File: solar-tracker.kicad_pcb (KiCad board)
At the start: 2 copper layers, 25 parts, among them J1 LDR1, J2 LDR2, J3 Motor, J4 Power, Q1 TIP41C, Q2 TIP41C, Q3 TIP42C, Q4 TIP42C, U1 LM324

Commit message: Create PCB layout for blocks
Signed-off-by: Sam Protsenko <joe.skb7@gmail.com>
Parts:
- removed the REF** at (27.9, 25.4)
- removed the REF** at (273.1, 24.1)
- removed the REF** at (25.4, 153.7)
- removed the REF** at (274.3, 153.7)
- added REF**: 1pin, Connectors:1pin, F.Cu at (106.7, 34.3)
- added REF**: 1pin, Connectors:1pin, F.Cu at (228.6, 26.7)
- added REF**: 1pin, Connectors:1pin, F.Cu at (105.4, 163.8)
- added REF**: 1pin, Connectors:1pin, F.Cu at (251.5, 157.5)
- moved J4 116.9 mm to (262.9, 100.3), turned to 90 degrees
- moved D1 101.1 mm to (228.6, 74.9)
- moved D2 101.1 mm to (246.4, 74.9)
- moved Q2 100.6 mm to (254.0, 77.5)
- moved Q4 100.6 mm to (254.0, 118.1)
- moved J3 100.6 mm to (234.9, 97.8)
- moved Q1 100.6 mm to (221.0, 77.5)
- moved Q3 100.6 mm to (221.0, 118.1)
- moved D3 100.4 mm to (228.6, 105.4)
- moved D4 100.4 mm to (246.4, 105.4)
- moved RV2 81.6 mm to (61.0, 105.4), turned to 90 degrees
- moved RV1 78.2 mm to (61.0, 91.4), turned to 90 degrees
- moved R1 77.5 mm to (68.6, 88.9)
- moved R3 74.4 mm to (121.9, 116.8), turned to 90 degrees
- moved R2 70.3 mm to (68.6, 102.9)
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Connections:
- J4 pad 1: VCC -> GND
- J4 pad 2: GND -> VCC
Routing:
- net GND: track 33.0 -> 222.0 mm
- net VCC: track 33.0 -> 208.3 mm
- net Net-(Q2-Pad1): track 47.8 -> 186.7 mm, vias 0 -> 4
- net Net-(J1-Pad2): track 0.00 -> 64.5 mm, vias 0 -> 2
- net Net-(Q1-Pad1): track 47.8 -> 92.9 mm, vias 0 -> 2
- net Net-(R1-Pad2): track 0.00 -> 27.5 mm
- net Net-(R2-Pad1): track 0.00 -> 27.5 mm
- net Net-(C2-Pad1): track 0.00 -> 26.7 mm
- net Net-(R1-Pad1): track 0.00 -> 12.1 mm
- net Net-(D2-Pad2): track 49.6 -> 59.8 mm
- net Net-(D1-Pad2): track 49.5 -> 59.7 mm
- net Net-(U1-Pad8): track 0.00 -> 2.54 mm
- net Net-(U1-Pad13): track 0.00 -> 2.54 mm
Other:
- net class Default: clearance 0.5 -> 0.3; via_dia 1.2 -> 2.5; via_drill 0.8 -> 1
- net class Power removed
- rule trace_clearance: 0.5 -> 0.3

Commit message: Finish PCB
Signed-off-by: Sam Protsenko <joe.skb7@gmail.com>
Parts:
- moved REF** 150.8 mm to (127.0, 72.4)
- moved D1 148.2 mm to (88.9, 25.4)
- moved D2 148.2 mm to (106.7, 25.4)
- moved D3 148.2 mm to (88.9, 55.9)
- moved D4 148.2 mm to (106.7, 55.9)
- moved J3 148.2 mm to (95.2, 48.3)
- moved J4 148.2 mm to (123.2, 50.8)
- moved Q1 148.2 mm to (81.3, 27.9)
- moved Q2 148.2 mm to (114.3, 27.9)
- moved Q3 148.2 mm to (81.3, 68.6)
- moved Q4 148.2 mm to (114.3, 68.6)
- moved REF** 125.8 mm to (19.1, 72.4)
- moved REF** 101.7 mm to (127.0, 21.6)
- moved REF** 88.5 mm to (19.1, 21.6)
- moved C1 79.0 mm to (52.1, 62.2)
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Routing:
- net Net-(Q2-Pad1): track 186.7 -> 208.2 mm
- net VCC: track 208.3 -> 221.0 mm
- net GND: track 222.0 -> 232.6 mm
- net Net-(Q1-Pad1): track 92.9 -> 94.5 mm

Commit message: pcb: Add PCB edges and copper pour
Signed-off-by: Sam Protsenko <joe.skb7@gmail.com>
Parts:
- moved ? 2.54 mm to (19.1, 69.8)
- moved C2 2.54 mm to (67.3, 41.9)
- moved REF** 2.54 mm to (127.0, 69.8)
- moved Q1 2.54 mm to (81.3, 25.4)
- moved Q2 2.54 mm to (114.3, 25.4)
- moved C1 2.54 mm to (52.1, 59.7)
- moved D1 2.54 mm to (88.9, 22.9)
- moved D2 2.54 mm to (106.7, 22.9)
- moved D3 2.54 mm to (88.9, 53.3)
- moved D4 2.54 mm to (106.7, 53.3)
- moved J1 2.54 mm to (22.9, 34.3)
- moved J2 2.54 mm to (22.9, 48.3)
- moved J3 2.54 mm to (95.2, 45.7)
- moved J4 2.54 mm to (123.2, 48.3)
- moved R1 2.54 mm to (39.4, 31.8)
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- renumbered REF** to ?
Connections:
- ? pad : (no net) -> GND
- REF** pad : (no net) -> GND (x3)
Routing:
- added copper zone on B.Cu, net GND
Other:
- board outline added: 115.6 x 58.4 mm

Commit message: pcb: Reduce via size
Signed-off-by: Sam Protsenko <joe.skb7@gmail.com>
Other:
- net class Default: via_dia 2.5 -> 2
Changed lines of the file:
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@@
     (links 51)
     (no_connects 0)
-    (area 15.24 14.927 130.810001 74.025)
+    (area 15.189999 14.927 130.860001 74.025)
     (thickness 1.6)
     (drawings 4)
@@
     (0 F.Cu signal)
     (31 B.Cu signal)
-    (33 F.Adhes user)
-    (35 F.Paste user)
+    (33 F.Adhes user hide)
+    (35 F.Paste user hide)
     (37 F.SilkS user)
-    (39 F.Mask user)
-    (40 Dwgs.User user)
-    (41 Cmts.User user)
-    (42 Eco1.User user)
-    (43 Eco2.User user)
+    (39 F.Mask user hide)
+    (40 Dwgs.User user hide)
+    (41 Cmts.User user hide)
+    (42 Eco1.User user hide)
+    (43 Eco2.User user hide)
     (44 Edge.Cuts user)
-    (45 Margin user)
+    (45 Margin user hide)
     (47 F.CrtYd user)
-    (49 F.Fab user)
+    (49 F.Fab user hide)
   )
   (setup
@@
     (segment_width 0.2)
     (edge_width 0.1)
-    (via_size 2.5)
+    (via_size 2)
     (via_drill 1)
     (via_min_size 0.4)
@@
     (visible_elements FFFFEF7F)
     (pcbplotparams
-      (layerselection 0x00030_80000001)
+      (layerselection 0x00020_80000001)
       (usegerberextensions false)
       (excludeedgelayer true)
@@
       (outputformat 1)
       (mirror false)
-      (drillshape 1)
+      (drillshape 0)
       (scaleselection 1)
-      (outputdirectory ""))
+      (outputdirectory ./))
   )
   (net 0 "")
@@
     (clearance 0.3)
     (trace_width 0.5)
-    (via_dia 2.5)
+    (via_dia 2)
     (via_drill 1)
     (uvia_dia 0.3)
@@
     (add_net "Net-(U1-Pad8)")
     (add_net VCC)
+  )
+  (module Connectors:1pin (layer F.Cu)
+    (at 19.05 19.05)
+    (descr "module 1 pin (ou trou mecanique de percage)")
+    (tags DEV)
+    (fp_text reference REF** (at 0 -3.048) (layer F.SilkS) hide
+      (effects (font (size 1 1) (thickness 0.15)))
+    )
+    (fp_text value 1pin (at 0 3) (layer F.Fab) hide
+      (effects (font (size 1 1) (thickness 0.15)))
+    )
+    (fp_circle (center 0 0) (end 2 0.8) (layer F.Fab) (width 0.1))
+    (fp_circle (center 0 0) (end 2.6 0) (layer F.CrtYd) (width 0.05))
+    (fp_circle (center 0 0) (end 0 -2.286) (layer F.SilkS) (width 0.12))
+    (pad "" thru_hole circle (at 0 0) (size 5 5) (drill 3.2) (layers *.Cu *.Mask)
+      (net 2 GND))
   )
   (module Housings_DIP:DIP-14_W7.62mm (layer F.Cu)
@@
   )
   (module Connectors:1pin (layer F.Cu)
-    (at 19.05 19.05)
-    (descr "module 1 pin (ou trou mecanique de percage)")
-    (tags DEV)
-    (fp_text reference REF** (at 0 -3.048) (layer F.SilkS) hide
-      (effects (font (size 1 1) (thickness 0.15)))
-    )
-    (fp_text value 1pin (at 0 3) (layer F.Fab) hide
-      (effects (font (size 1 1) (thickness 0.15)))
-    )
-    (fp_circle (center 0 0) (end 2 0.8) (layer F.Fab) (width 0.1))
-    (fp_circle (center 0 0) (end 2.6 0) (layer F.CrtYd) (width 0.05))
-    (fp_circle (center 0 0) (end 0 -2.286) (layer F.SilkS) (width 0.12))
-    (pad "" thru_hole circle (at 0 0) (size 5 5) (drill 3.2) (layers *.Cu *.Mask)
-      (net 2 GND))
-  )
-  (module Connectors:1pin (layer F.Cu)
     (at 127 19.05)
     (descr "module 1 pin (ou trou mecanique de percage)")
@@
   (segment (start 50.8 44.45) (end 46.99 44.45) (width 0.5) (layer B.Cu) (net 6))
   (segment (start 46.99 52.07) (end 50.8 52.07) (width 0.5) (layer B.Cu) (net 6))
-  (via (at 46.99 52.07) (size 2.5) (drill 1) (layers F.Cu B.Cu) (net 6))
+  (via (at 46.99 52.07) (size 2) (drill 1) (layers F.Cu B.Cu) (net 6))
   (segment (start 46.99 44.45) (end 46.99 52.07) (width 0.5) (layer F.Cu) (net 6))
-  (via (at 46.99 44.45) (size 2.5) (drill 1) (layers F.Cu B.Cu) (net 6))
+  (via (at 46.99 44.45) (size 2) (drill 1) (layers F.Cu B.Cu) (net 6))
   (segment (start 43.18 36.83) (end 43.18 36.83) (width 0.5) (layer B.Cu) (net 6))
   (segment (start 22.86 43.18) (end 33.02 43.18) (width 0.5) (layer B.Cu) (net 6))
@@
   (segment (start 46.99 27.94) (end 46.99 39.37) (width 0.5) (layer F.Cu) (net 7))
   (segment (start 77.47 27.94) (end 68.58 27.94) (width 0.5) (layer B.Cu) (net 7))
-  (via (at 46.99 39.37) (size 2.5) (drill 1) (layers F.Cu B.Cu) (net 7))
-  (via (at 46.99 27.94) (size 2.5) (drill 1) (layers F.Cu B.Cu) (net 7))
+  (via (at 46.99 39.37) (size 2) (drill 1) (layers F.Cu B.Cu) (net 7))
+  (via (at 46.99 27.94) (size 2) (drill 1) (layers F.Cu B.Cu) (net 7))
   (segment (start 46.99 39.37) (end 50.8 39.37) (width 0.5) (layer B.Cu) (net 7))
   (segment (start 46.99 27.94) (end 68.58 27.94) (width 0.5) (layer B.Cu) (net 7))
@@
   (segment (start 49.53 55.88) (end 49.53 63.5) (width 0.5) (layer B.Cu) (net 8))
   (segment (start 49.53 63.5) (end 50.8 64.77) (width 0.5) (layer B.Cu) (net 8))
-  (via (at 67.31 64.77) (size 2.5) (drill 1) (layers F.Cu B.Cu) (net 8))
+  (via (at 67.31 64.77) (size 2) (drill 1) (layers F.Cu B.Cu) (net 8))
   (segment (start 50.8 64.77) (end 67.31 64.77) (width 0.5) (layer B.Cu) (net 8))
   (segment (start 67.31 64.77) (end 73.66 64.77) (width 0.5) (layer F.Cu) (net 8))
-  (via (at 73.66 64.77) (size 2.5) (drill 1) (layers F.Cu B.Cu) (net 8))
-  (via (at 73.66 33.02) (size 2.5) (drill 1) (layers F.Cu B.Cu) (net 8))
+  (via (at 73.66 64.77) (size 2) (drill 1) (layers F.Cu B.Cu) (net 8))
+  (via (at 73.66 33.02) (size 2) (drill 1) (layers F.Cu B.Cu) (net 8))
   (segment (start 125.73 26.67) (end 118.11 19.05) (width 0.5) (layer B.Cu) (net 8))
   (segment (start 125.73 27.305332) (end 125.73 26.67) (width 0.5) (layer B.Cu) (net 8))
@@
   (segment (start 119.38 45.72) (end 125.73 45.72) (width 0.5) (layer B.Cu) (net 8))
   (segment (start 118.11 19.05) (end 73.66 19.05) (width 0.5) (layer B.Cu) (net 8))
-  (via (at 73.66 19.05) (size 2.5) (drill 1) (layers F.Cu B.Cu) (net 8))
+  (via (at 73.66 19.05) (size 2) (drill 1) (layers F.Cu B.Cu) (net 8))
   (segment (start 73.66 19.05) (end 73.66 33.02) (width 0.5) (layer F.Cu) (net 8))
   (segment (start 119.38 45.72) (end 119.38 63.5) (width 0.5) (layer B.Cu) (net 8))

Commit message: pcb: Remove copper pour
Prepare PCB for LUT (toner transfer method).

Signed-off-by: Sam Protsenko <joe.skb7@gmail.com>
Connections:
- ? pad : GND -> (no net)
- REF** pad : GND -> (no net) (x3)
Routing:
- removed copper zone on B.Cu, net GND
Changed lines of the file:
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@@
 (kicad_pcb (version 4) (host pcbnew 4.0.7+dfsg1-1)
   (general
-    (links 51)
+    (links 47)
     (no_connects 0)
-    (area 15.189999 14.927 130.860001 74.025)
+    (area 15.189999 15.189999 130.860001 73.710001)
     (thickness 1.6)
     (drawings 4)
@@
       (padsonsilk false)
       (subtractmaskfromsilk false)
-      (outputformat 1)
+      (outputformat 5)
       (mirror false)
       (drillshape 0)
@@
     (fp_circle (center 0 0) (end 2.6 0) (layer F.CrtYd) (width 0.05))
     (fp_circle (center 0 0) (end 0 -2.286) (layer F.SilkS) (width 0.12))
-    (pad "" thru_hole circle (at 0 0) (size 5 5) (drill 3.2) (layers *.Cu *.Mask)
-      (net 2 GND))
+    (pad "" thru_hole circle (at 0 0) (size 5 5) (drill 3.2) (layers *.Cu *.Mask))
   )
   (module Housings_DIP:DIP-14_W7.62mm (layer F.Cu)
@@
     (fp_circle (center 0 0) (end 2.6 0) (layer F.CrtYd) (width 0.05))
     (fp_circle (center 0 0) (end 0 -2.286) (layer F.SilkS) (width 0.12))
-    (pad "" thru_hole circle (at 0 0) (size 5 5) (drill 3.2) (layers *.Cu *.Mask)
-      (net 2 GND))
+    (pad "" thru_hole circle (at 0 0) (size 5 5) (drill 3.2) (layers *.Cu *.Mask))
   )
   (module Connectors:1pin (layer F.Cu)
@@
     (fp_circle (center 0 0) (end 2.6 0) (layer F.CrtYd) (width 0.05))
     (fp_circle (center 0 0) (end 0 -2.286) (layer F.SilkS) (width 0.12))
-    (pad "" thru_hole circle (at 0 0) (size 5 5) (drill 3.2) (layers *.Cu *.Mask)
-      (net 2 GND))
+    (pad "" thru_hole circle (at 0 0) (size 5 5) (drill 3.2) (layers *.Cu *.Mask))
   )
   (module Connectors:1pin (layer F.Cu)
@@
     (fp_circle (center 0 0) (end 2.6 0) (layer F.CrtYd) (width 0.05))
     (fp_circle (center 0 0) (end 0 -2.286) (layer F.SilkS) (width 0.12))
-    (pad "" thru_hole circle (at 0 0) (size 5 5) (drill 3.2) (layers *.Cu *.Mask)
-      (net 2 GND))
+    (pad "" thru_hole circle (at 0 0) (size 5 5) (drill 3.2) (layers *.Cu *.Mask))
   )
   (gr_line (start 130.81 15.24) (end 15.24 15.24) (layer Edge.Cuts) (width 0.1))
@@
   (segment (start 58.42 52.07) (end 58.42 54.61) (width 0.5) (layer B.Cu) (net 12))
   (segment (start 58.42 39.37) (end 58.42 41.91) (width 0.5) (layer B.Cu) (net 13))
-  (zone (net 2) (net_name GND) (layer B.Cu) (hatch edge 0.508)
-    (connect_pads (clearance 0.508))
-    (min_thickness 0.254)
-    (fill yes (arc_segments 16) (thermal_gap 1.016) (thermal_bridge_width 0.508))
-    (polygon
-      (pts
-        (xy 130.81 73.66) (xy 15.24 73.66) (xy 15.24 15.24) (xy 130.81 15.24)
-      )
-    )
-  )
 )

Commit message: pcb: Bring C1 close to H-bridge
Signed-off-by: Sam Protsenko <joe.skb7@gmail.com>
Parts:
- moved C1 71.7 mm to (121.9, 43.2), turned to 270 degrees
- moved REF** 7.62 mm to (134.6, 19.1)
- moved REF** 7.62 mm to (134.6, 69.8)
- moved J4 6.35 mm to (129.5, 48.3)
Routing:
- net Net-(Q2-Pad1): track 208.2 -> 217.2 mm
- net GND: track 232.6 -> 239.2 mm
- net VCC: track 221.0 -> 225.7 mm
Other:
- board size 115.6 x 58.4 mm -> 123.2 x 58.4 mm

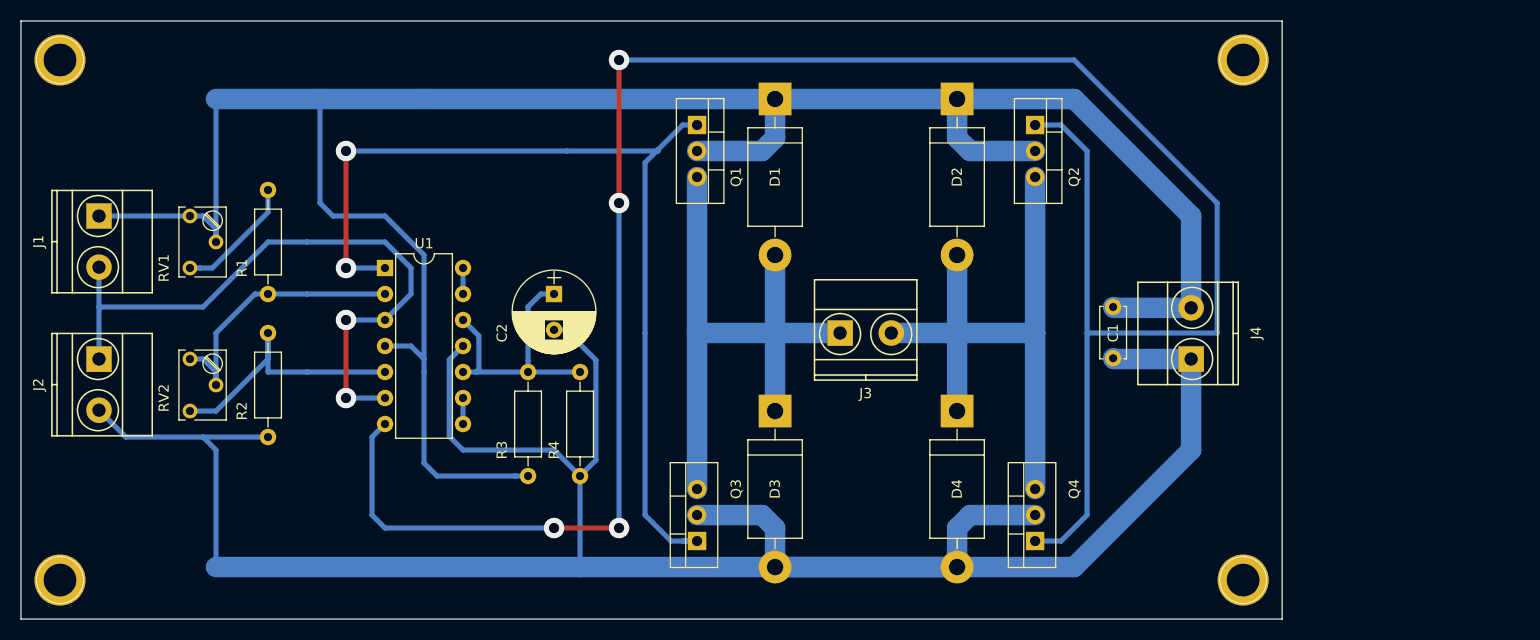
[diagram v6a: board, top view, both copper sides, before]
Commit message: Update schematic and PCB to Revision B
- Add limit switches + diodes
- Vcc -> 9V
- Use JST XH connectors for photo-resistors (instead of screw terminal
  blocks)
- Add mounting holes to schematic
- Bring back the copper pour; for Toner Transfer Method one can simply
  remove it
- Add copper pour for front layer (F.Cu)
- Add +/- labels for power and motor terminal blocks

Signed-off-by: Sam Protsenko <joe.skb7@gmail.com>
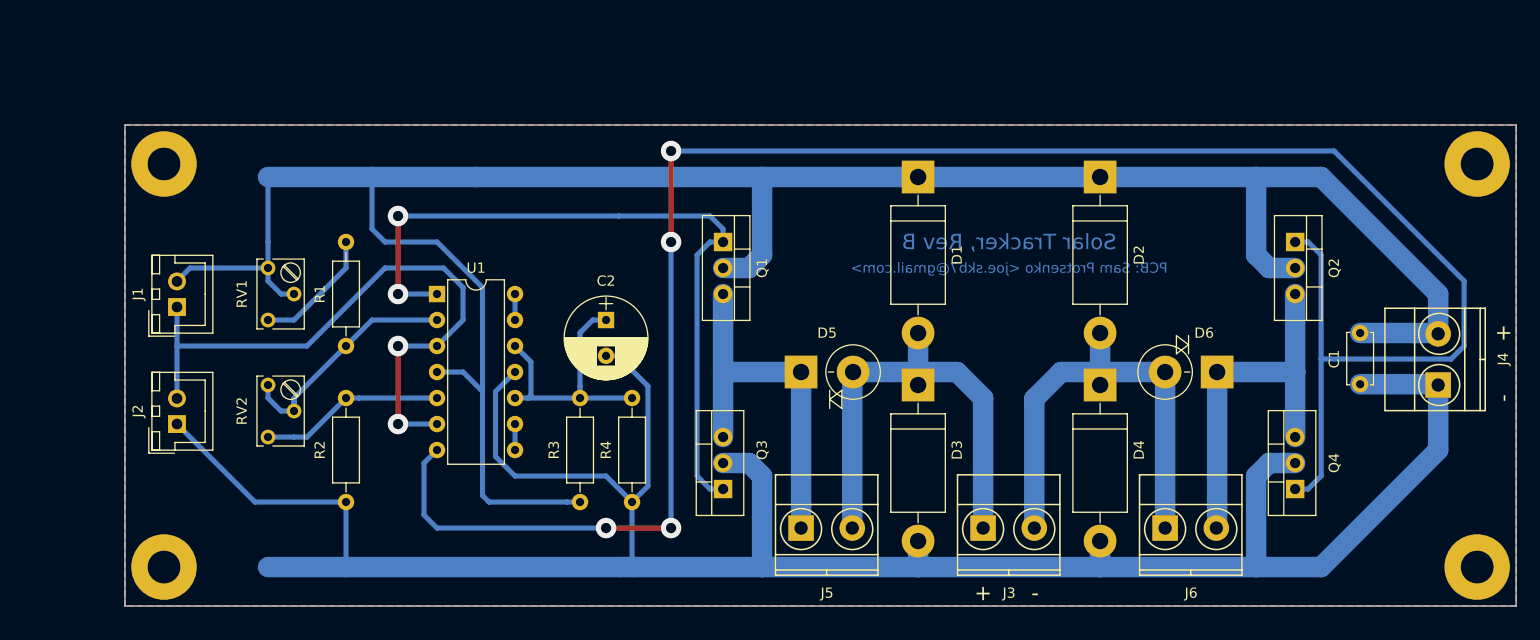
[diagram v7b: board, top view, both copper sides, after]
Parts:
- removed ?, REF** (x3): 1pin, Connectors:1pin
- added D5: 1N5402, Diodes_THT:D_DO-201AD_P5.08mm_Vertical_KathodeUp, F.Cu at (91.4, 49.5)
- added D6: 1N5402, Diodes_THT:D_DO-201AD_P5.08mm_Vertical_KathodeUp, F.Cu at (132.1, 49.5)
- added J5: FWD_Limit, Connectors_Terminal_Blocks:TerminalBlock_Pheonix_MKDS1.5-2pol, F.Cu at (91.4, 64.8)
- added J6: REV_Limit, Connectors_Terminal_Blocks:TerminalBlock_Pheonix_MKDS1.5-2pol, F.Cu at (127.0, 64.8)
- added MK1: Mounting_Hole_PAD, Mounting_Holes:MountingHole_3.2mm_M3_Pad, F.Cu at (29.2, 29.2)
- added MK2: Mounting_Hole_PAD, Mounting_Holes:MountingHole_3.2mm_M3_Pad, F.Cu at (157.5, 29.2)
- added MK3: Mounting_Hole_PAD, Mounting_Holes:MountingHole_3.2mm_M3_Pad, F.Cu at (29.2, 68.6)
- added MK4: Mounting_Hole_PAD, Mounting_Holes:MountingHole_3.2mm_M3_Pad, F.Cu at (157.5, 68.6)
- J1, J2: footprint Connectors_Terminal_Blocks:TerminalBlock_Pheonix_MKDS1.5-2pol -> Connectors_JST:JST_XH_B02B-XH-A_02x2.50mm_Straight
- J4: value Power -> Power_9V
- moved Q2 27.9 mm to (139.7, 36.8)
- moved Q4 25.9 mm to (139.7, 61.0)
- moved C1 24.3 mm to (146.1, 45.7)
- moved J4 24.3 mm to (153.7, 50.8)
- moved J3 23.6 mm to (109.2, 64.8)
- moved D1 15.9 mm to (102.9, 30.5)
- moved D2 15.9 mm to (120.7, 30.5)
- moved D3 14.2 mm to (102.9, 50.8)
- moved D4 14.2 mm to (120.7, 50.8)
- moved J1 11.7 mm to (30.5, 43.2), turned to 90 degrees
- moved Q1 11.7 mm to (83.8, 36.8)
- moved R2 9.92 mm to (47.0, 52.1)
- moved J2 9.92 mm to (30.5, 54.6), turned to 90 degrees
- moved R1 9.16 mm to (47.0, 36.8)
- moved RV1 9.16 mm to (39.4, 39.4)
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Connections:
- C1 pad 1: VCC -> +9V
- D1 pad 1: VCC -> +9V
- D2 pad 1: VCC -> +9V
- J1 pad 1: VCC -> Net-(J1-Pad1)
- J1 pad 2: Net-(J1-Pad2) -> +9V
- J2 pad 1: Net-(J1-Pad2) -> GND
- J2 pad 2: GND -> Net-(J1-Pad1)
- J4 pad 2: VCC -> +9V
- Q1 pad 2: VCC -> +9V
- Q1 pad 3: Net-(D1-Pad2) -> Net-(D5-Pad1)
- Q2 pad 2: VCC -> +9V
- Q2 pad 3: Net-(D2-Pad2) -> Net-(D6-Pad1)
- Q3 pad 3: Net-(D1-Pad2) -> Net-(D5-Pad1)
- Q4 pad 3: Net-(D2-Pad2) -> Net-(D6-Pad1)
- R3 pad 1: VCC -> +9V
- RV1 pad 1: VCC -> +9V
- RV1 pad 2: VCC -> +9V
- U1 pad 3: Net-(J1-Pad2) -> Net-(J1-Pad1)
- U1 pad 4: VCC -> +9V
- U1 pad 6: Net-(J1-Pad2) -> Net-(J1-Pad1)
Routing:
- net +9V: track 0.00 -> 230.8 mm
- net VCC: track 225.7 -> 0.00 mm
- net Net-(J1-Pad2): track 64.5 -> 0.00 mm, vias 2 -> 0
- net Net-(J1-Pad1): track 0.00 -> 62.8 mm, vias 0 -> 2
- net Net-(D6-Pad1): track 0.00 -> 37.0 mm
- net Net-(D5-Pad1): track 0.00 -> 36.8 mm
- net Net-(Q1-Pad1): track 94.5 -> 72.7 mm
- net Net-(Q2-Pad1): track 217.2 -> 199.7 mm
- net Net-(D2-Pad2): track 59.8 -> 46.8 mm
- net Net-(D1-Pad2): track 59.7 -> 46.9 mm
- net Net-(R2-Pad1): track 27.5 -> 18.1 mm
- net Net-(R1-Pad2): track 27.5 -> 23.8 mm
- net GND: track 239.2 -> 238.4 mm
- net Net-(R1-Pad1): track 12.1 -> 12.6 mm
- added copper zone on B.Cu, net GND
- added copper zone on F.Cu, net GND
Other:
- board size 123.2 x 58.4 mm -> 135.9 x 47 mm
- net class Default: clearance 0.3 -> 0.5
- rule trace_clearance: 0.3 -> 0.5
- rule trace_min: 0.2 -> 0.5
- board text added: "+"
- board text added: "-"
- board text added: "PCB: Sam Protsenko <joe.skb7@gmail.com>"
- board text added: "Solar Tracker, Rev B"
